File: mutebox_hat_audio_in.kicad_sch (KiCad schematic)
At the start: 39 parts, among them J1 GPIO, J3 RCJ-042, J4 RCJ-042, U2 74LVC157, U3 PCM1862DBT, Y3 XO32

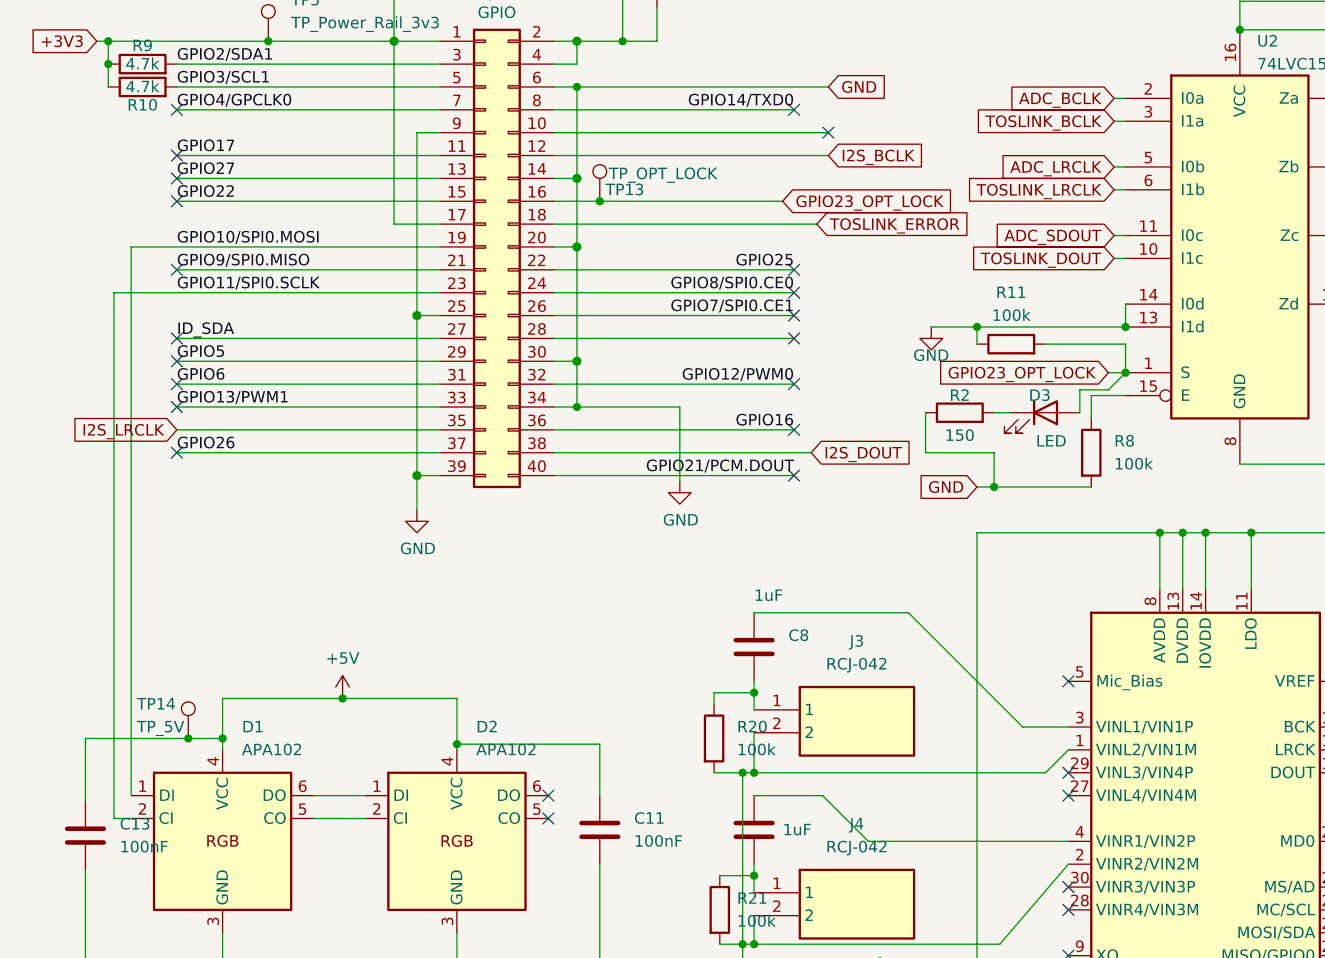
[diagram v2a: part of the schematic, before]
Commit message: Moved dotstar caps to front of board.
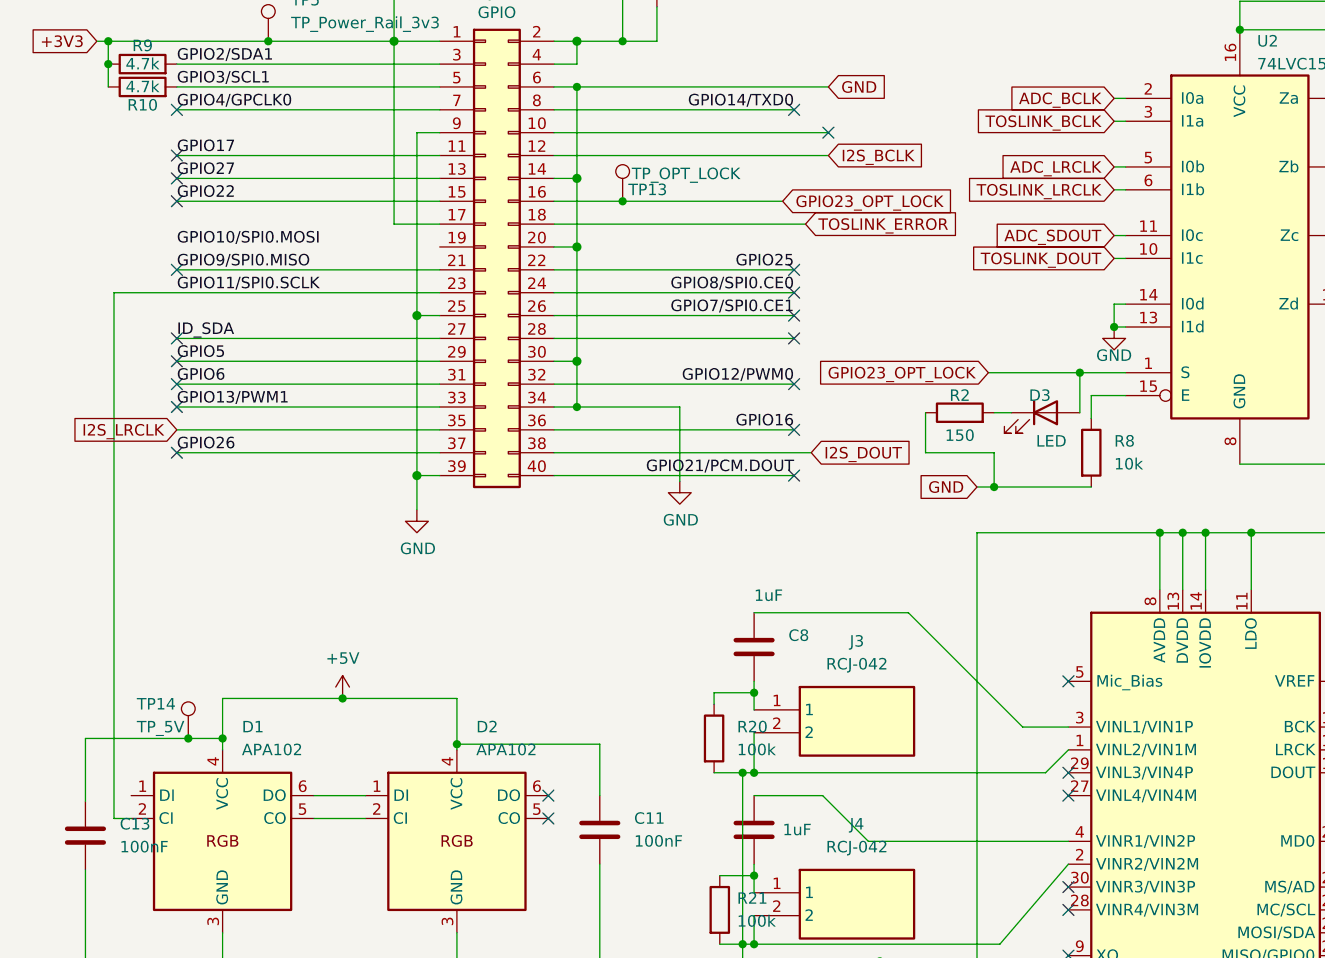
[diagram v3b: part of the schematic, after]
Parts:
- removed R11: 100k, Resistor_SMD:R_0805_2012Metric_Pad1.20x1.40mm_HandSolder, symbol Device:R
- R8: value 100k -> 10k
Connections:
- net GPIO10/SPI0.MOSI: no longer D1.1 (DI), J1.19 (Pin_19)
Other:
- moved on the sheet: TP13

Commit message: Fixed RCA Jack LCSC part numbers
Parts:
- J3, J4: LCSC C28323 -> C22359751
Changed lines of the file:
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@@
 			)
 		)
-		(property "LCSC" "C28323"
+		(property "LCSC" "C22359751"
 			(at 95.885 102.235 0)
 			(effects
@@
 			)
 		)
-		(property "LCSC" "C28323"
+		(property "LCSC" "C22359751"
 			(at 95.885 122.555 0)
 			(effects

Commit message: Final changes before ordering.
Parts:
- added R3: 0, Resistor_SMD:R_0805_2012Metric_Pad1.20x1.40mm_HandSolder, symbol Device:R
- D3: value LED -> NCD0805R1
- J1, TP14: now left out of the parts list
- J3, J4, TP1, TP10, TP11, TP12, TP13, TP2, TP3, TP5: DNP (none) -> 1; now left out of the parts list
- R2: LCSC (none) -> C17471
- R8: LCSC C149504 -> C17414
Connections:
- net GND: now also R3.1; no longer J3.2, J4.2, R20.2, R21.2, U3.1 (VINL2/VIN1M), U3.2 (VINR2/VIN2M)
- new net: J3.2, J4.2, R20.2, R21.2, R3.2, U3.1 (VINL2/VIN1M), U3.2 (VINR2/VIN2M)
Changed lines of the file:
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@@
 	(wire
 		(pts
+			(xy 94.615 139.065) (xy 94.615 128.27)
+		)
+		(stroke
+			(width 0)
+			(type default)
+		)
+	)
+	(wire
+		(pts
 			(xy 162.56 34.29) (xy 167.64 34.29)
 		)
@@
 	(wire
 		(pts
-			(xy 94.615 156.21) (xy 94.615 128.27)
+			(xy 94.615 156.21) (xy 94.615 146.685)
 		)
 		(stroke
@@
 		(unit 1)
 		(exclude_from_sim no)
-		(in_bom yes)
+		(in_bom no)
 		(on_board yes)
 		(dnp no)
@@
 	)
 	(symbol
+		(lib_id "Device:R")
+		(at 94.615 142.875 180)
+		(unit 1)
+		(exclude_from_sim no)
+		(in_bom yes)
+		(on_board yes)
+		(dnp no)
+		(fields_autoplaced yes)
+		(property "Reference" "R3"
+			(at 96.52 141.6049 0)
+			(effects
+				(font
+					(size 1.27 1.27)
+				)
+				(justify right)
+			)
+		)
+		(property "Value" "0"
+			(at 96.52 144.1449 0)
+			(effects
+				(font
+					(size 1.27 1.27)
+				)
+				(justify right)
+			)
+		)
+		(property "Footprint" "Resistor_SMD:R_0805_2012Metric_Pad1.20x1.40mm_HandSolder"
+			(at 96.393 142.875 90)
+			(effects
+				(font
+					(size 1.27 1.27)
+				)
+				(hide yes)
+			)
+		)
+		(property "Datasheet" "~"
+			(at 94.615 142.875 0)
+			(effects
+				(font
+					(size 1.27 1.27)
+				)
+				(hide yes)
+			)
+		)
+		(property "Description" "Resistor"
+			(at 94.615 142.875 0)
+			(effects
+				(font
+					(size 1.27 1.27)
+				)
+				(hide yes)
+			)
+		)
+		(property "LCSC" "C98220"
+			(at 94.615 142.875 90)
+			(effects
+				(font
+					(size 1.27 1.27)
+				)
+				(hide yes)
+			)
+		)
+		(pin "1"
+		)
+		(pin "2"
+		)
+		(instances
+			(project "mutebox_hat_audio_in"
+				(path "/e63e39d7-6ac0-4ffd-8aa3-1841a4541b55"
+					(reference "R3")
+					(unit 1)
+				)
+			)
+		)
+	)
+	(symbol
 		(lib_id "APA102:APA102")
 		(at 36.83 116.84 0)
@@
 			)
 		)
-		(property "Value" "LED"
+		(property "Value" "NCD0805R1"
 			(at 128.905 72.39 0)
 			(effects
@@
 		(unit 1)
 		(exclude_from_sim no)
-		(in_bom yes)
+		(in_bom no)
 		(on_board yes)
 		(dnp no)
@@
 			)
 		)
+		(property "DNP" "1"
+			(at 162.56 104.14 0)
+			(effects
+				(font
+					(size 1.27 1.27)
+				)
+				(hide yes)
+			)
+		)
 		(pin "1"
 		)
@@
 		(unit 1)
 		(exclude_from_sim no)
-		(in_bom yes)
+		(in_bom no)
 		(on_board yes)
 		(dnp no)
@@
 			)
 		)
+		(property "DNP" "1"
+			(at 162.56 41.91 0)
+			(effects
+				(font
+					(size 1.27 1.27)
+				)
+				(hide yes)
+			)
+		)
 		(pin "1"
 		)
@@
 		(unit 1)
 		(exclude_from_sim no)
-		(in_bom yes)
+		(in_bom no)
 		(on_board yes)
 		(dnp no)
@@
 			)
 		)
+		(property "DNP" "1"
+			(at 95.885 102.235 0)
+			(effects
+				(font
+					(size 1.27 1.27)
+				)
+				(hide yes)
+			)
+		)
 		(pin "1"
 		)
@@
 			)
 		)
+		(property "LCSC" "C17471"
+			(at 118.745 69.215 90)
+			(effects
+				(font
+					(size 1.27 1.27)
+				)
+				(hide yes)
+			)
+		)
 		(pin "2"
 		)
@@
 		(unit 1)
 		(exclude_from_sim no)
-		(in_bom yes)
+		(in_bom no)
 		(on_board yes)
 		(dnp no)
@@
 		(unit 1)
 		(exclude_from_sim no)
-		(in_bom yes)
+		(in_bom no)
 		(on_board yes)
 		(dnp no)
@@
 			)
 		)
+		(property "DNP" "1"
+			(at 41.91 27.94 0)
+			(effects
+				(font
+					(size 1.27 1.27)
+				)
+				(hide yes)
+			)
+		)
 		(pin "1"
 		)
@@
 		(unit 1)
 		(exclude_from_sim no)
-		(in_bom yes)
+		(in_bom no)
 		(on_board yes)
 		(dnp no)
@@
 			)
 		)
+		(property "DNP" "1"
+			(at 162.56 34.29 0)
+			(effects
+				(font
+					(size 1.27 1.27)
+				)
+				(hide yes)
+			)
+		)
 		(pin "1"
 		)
@@
 		(unit 1)
 		(exclude_from_sim no)
-		(in_bom yes)
+		(in_bom no)
 		(on_board yes)
 		(dnp no)
@@
 			)
 		)
+		(property "DNP" "1"
+			(at 162.56 49.53 0)
+			(effects
+				(font
+					(size 1.27 1.27)
+				)
+				(hide yes)
+			)
+		)
 		(pin "1"
 		)
@@
 		(unit 1)
 		(exclude_from_sim no)
-		(in_bom yes)
+		(in_bom no)
 		(on_board yes)
 		(dnp no)
@@
 			)
 		)
+		(property "DNP" "1"
+			(at 95.885 122.555 0)
+			(effects
+				(font
+					(size 1.27 1.27)
+				)
+				(hide yes)
+			)
+		)
 		(pin "1"
 		)
@@
 		(unit 1)
 		(exclude_from_sim no)
-		(in_bom yes)
+		(in_bom no)
 		(on_board yes)
 		(dnp no)
@@
 			)
 		)
+		(property "DNP" "1"
+			(at 81.28 45.72 0)
+			(effects
+				(font
+					(size 1.27 1.27)
+				)
+				(hide yes)
+			)
+		)
 		(pin "1"
 		)
@@
 		(unit 1)
 		(exclude_from_sim no)
-		(in_bom yes)
+		(in_bom no)
 		(on_board yes)
 		(dnp no)
@@
 			)
 		)
+		(property "DNP" "1"
+			(at 165.1 109.22 0)
+			(effects
+				(font
+					(size 1.27 1.27)
+				)
+				(hide yes)
+			)
+		)
 		(pin "1"
 		)
@@
 		(unit 1)
 		(exclude_from_sim no)
-		(in_bom yes)
+		(in_bom no)
 		(on_board yes)
 		(dnp no)
@@
 			)
 		)
+		(property "DNP" "1"
+			(at 163.83 106.68 0)
+			(effects
+				(font
+					(size 1.27 1.27)
+				)
+				(hide yes)
+			)
+		)
 		(pin "1"
 		)
@@
 			)
 		)
-		(property "LCSC" "C149504"
+		(property "LCSC" "C17414"
 			(at 133.35 73.66 0)
 			(effects

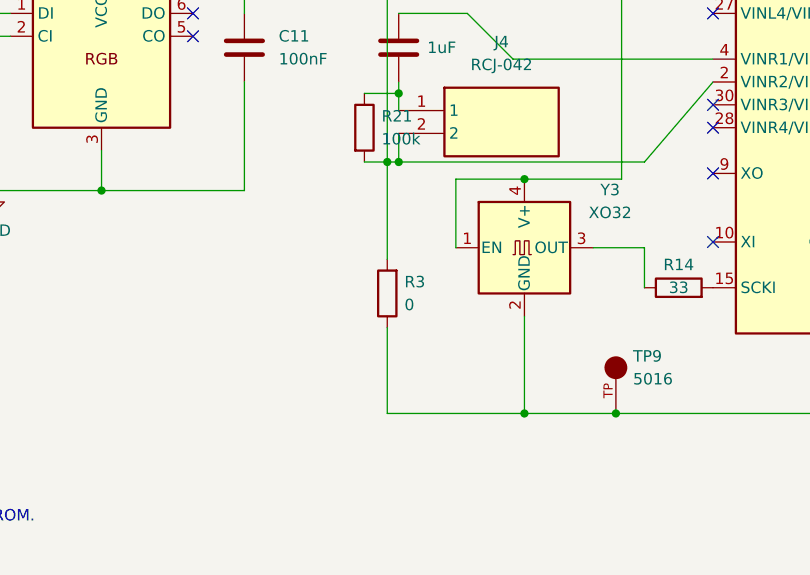
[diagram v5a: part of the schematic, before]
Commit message: Fixed missing connection from RPi4 to dotstar LED
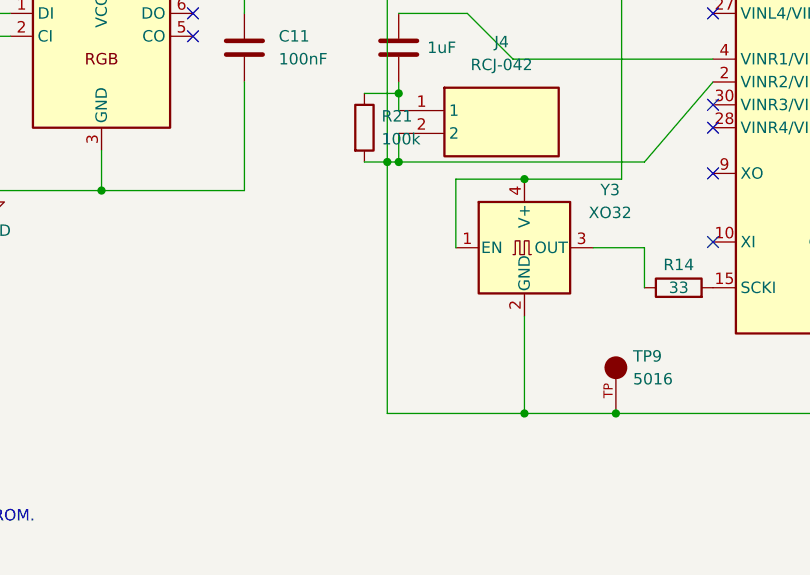
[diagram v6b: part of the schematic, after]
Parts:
- removed R3: 0, Resistor_SMD:R_0805_2012Metric_Pad1.20x1.40mm_HandSolder, symbol Device:R
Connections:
- net GND: now also J3.2, J4.2, R20.2, R21.2, U3.1 (VINL2/VIN1M), U3.2 (VINR2/VIN2M)
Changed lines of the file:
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@@
 	(wire
 		(pts
-			(xy 94.615 139.065) (xy 94.615 128.27)
+			(xy 94.615 128.27) (xy 94.615 156.21)
 		)
 		(stroke
@@
 		(pts
 			(xy 36.83 131.445) (xy 50.8 131.445)
-		)
-		(stroke
-			(width 0)
-			(type default)
-		)
-	)
-	(wire
-		(pts
-			(xy 94.615 156.21) (xy 94.615 146.685)
 		)
 		(stroke
@@
 					(unit 1)
 				)
-			)
-		)
-	)
-	(symbol
-		(lib_id "Device:R")
-		(at 94.615 142.875 180)
-		(unit 1)
-		(exclude_from_sim no)
-		(in_bom yes)
-		(on_board yes)
-		(dnp no)
-		(fields_autoplaced yes)
-		(property "Reference" "R3"
-			(at 96.52 141.6049 0)
-			(effects
-				(font
-					(size 1.27 1.27)
-				)
-				(justify right)
-			)
-		)
-		(property "Value" "0"
-			(at 96.52 144.1449 0)
-			(effects
-				(font
-					(size 1.27 1.27)
-				)
-				(justify right)
-			)
-		)
-		(property "Footprint" "Resistor_SMD:R_0805_2012Metric_Pad1.20x1.40mm_HandSolder"
-			(at 96.393 142.875 90)
-			(effects
-				(font
-					(size 1.27 1.27)
-				)
-				(hide yes)
-			)
-		)
-		(property "Datasheet" "~"
-			(at 94.615 142.875 0)
-			(effects
-				(font
-					(size 1.27 1.27)
-				)
-				(hide yes)
-			)
-		)
-		(property "Description" "Resistor"
-			(at 94.615 142.875 0)
-			(effects
-				(font
-					(size 1.27 1.27)
-				)
-				(hide yes)
-			)
-		)
-		(property "LCSC" "C98220"
-			(at 94.615 142.875 90)
-			(effects
-				(font
-					(size 1.27 1.27)
-				)
-				(hide yes)
-			)
-		)
-		(pin "1"
-		)
-		(pin "2"
-		)
-		(instances
-			(project "mutebox_hat_audio_in"
-				(path "/e63e39d7-6ac0-4ffd-8aa3-1841a4541b55"
-					(reference "R3")
-					(unit 1)
-				)

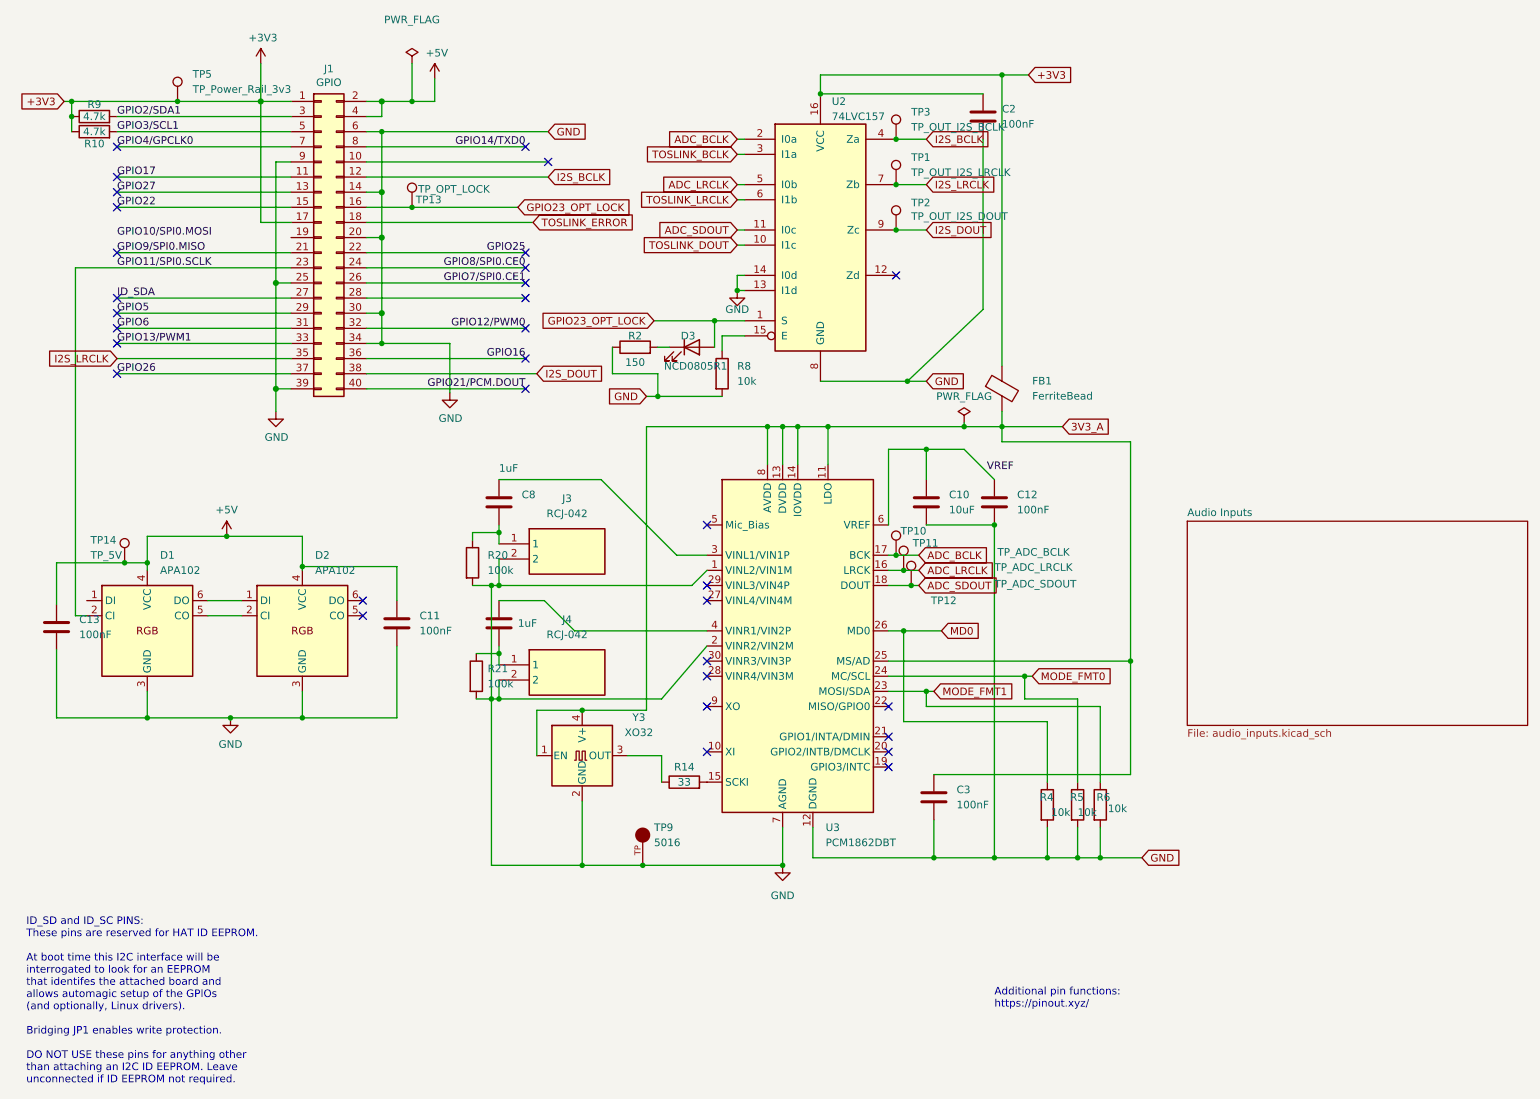
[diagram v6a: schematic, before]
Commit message: Changed MS/AD (pin 25) to go to GND for default address 0x4A
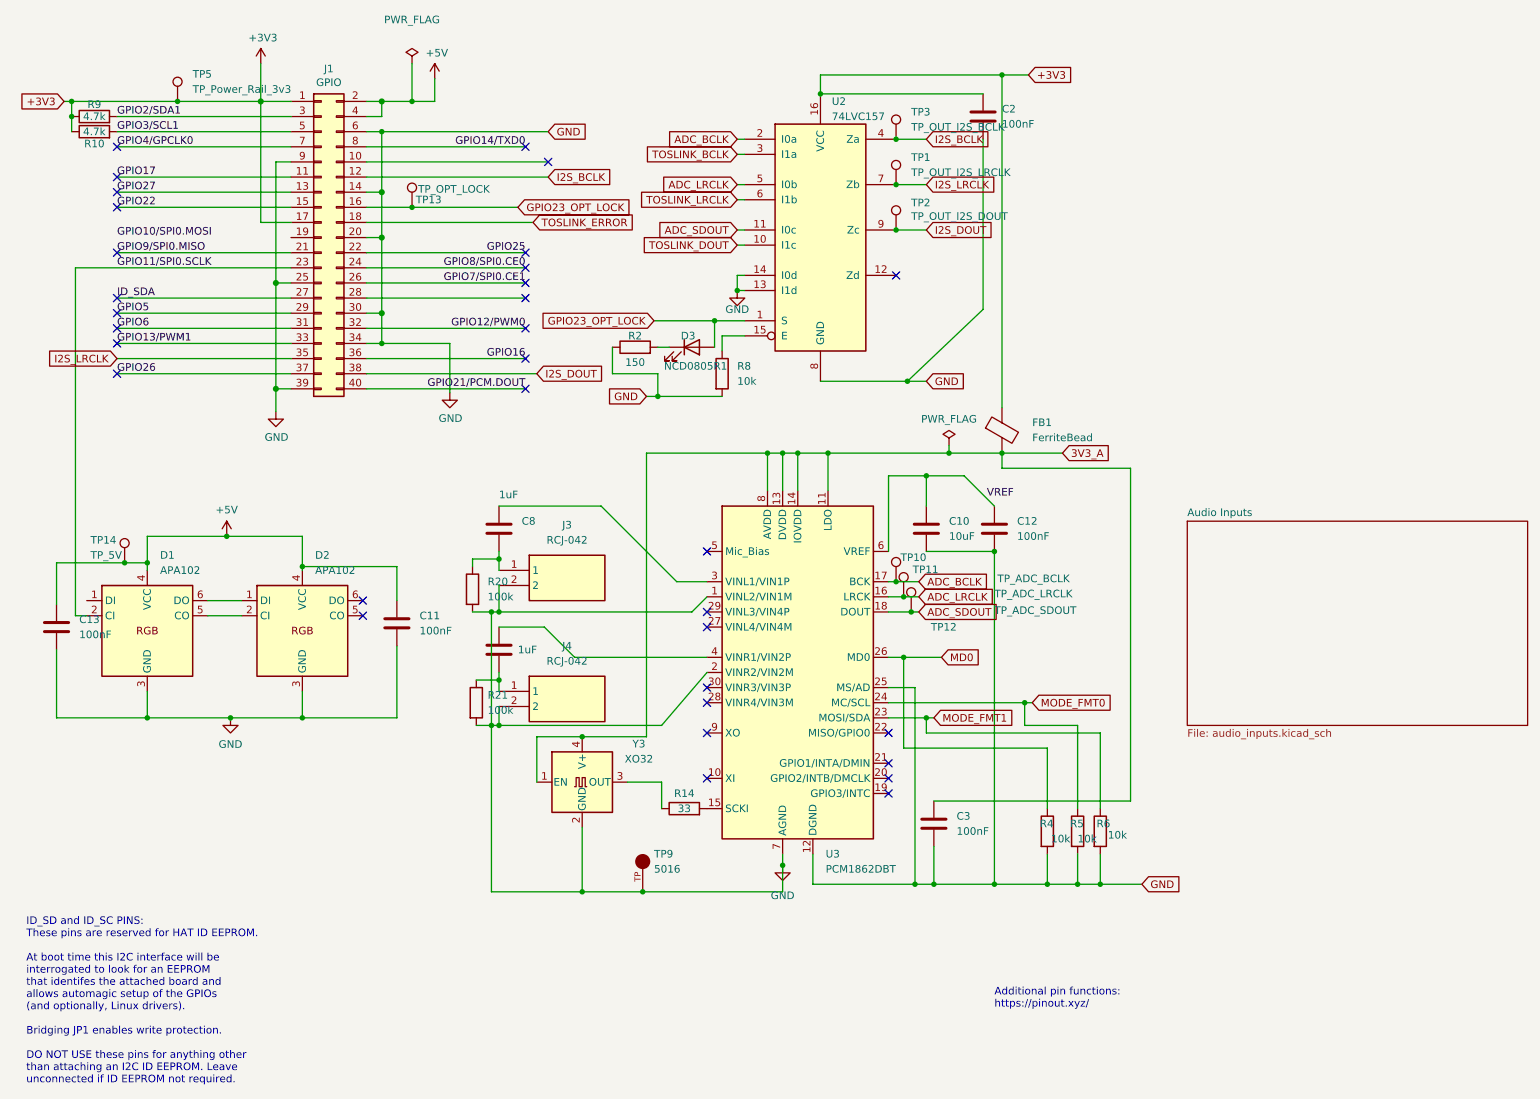
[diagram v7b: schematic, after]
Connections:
- net 3V3_A: no longer U3.25 (MS/AD)
- net GND: now also U3.25 (MS/AD)
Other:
- moved on the sheet: C10, C12, C3, C8, FB1, J3, J4, R14, R20, R21, R4, R5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
